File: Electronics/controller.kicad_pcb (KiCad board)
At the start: 2 copper layers, 70 x 50 mm, 21 parts, among them J101 Conn_01x06_Female, J102 Conn_01x06_Female, Q101 2N7002, Q102 2N7002, Q103 IRF9540NPBF, Q104 IRF9540NPBF

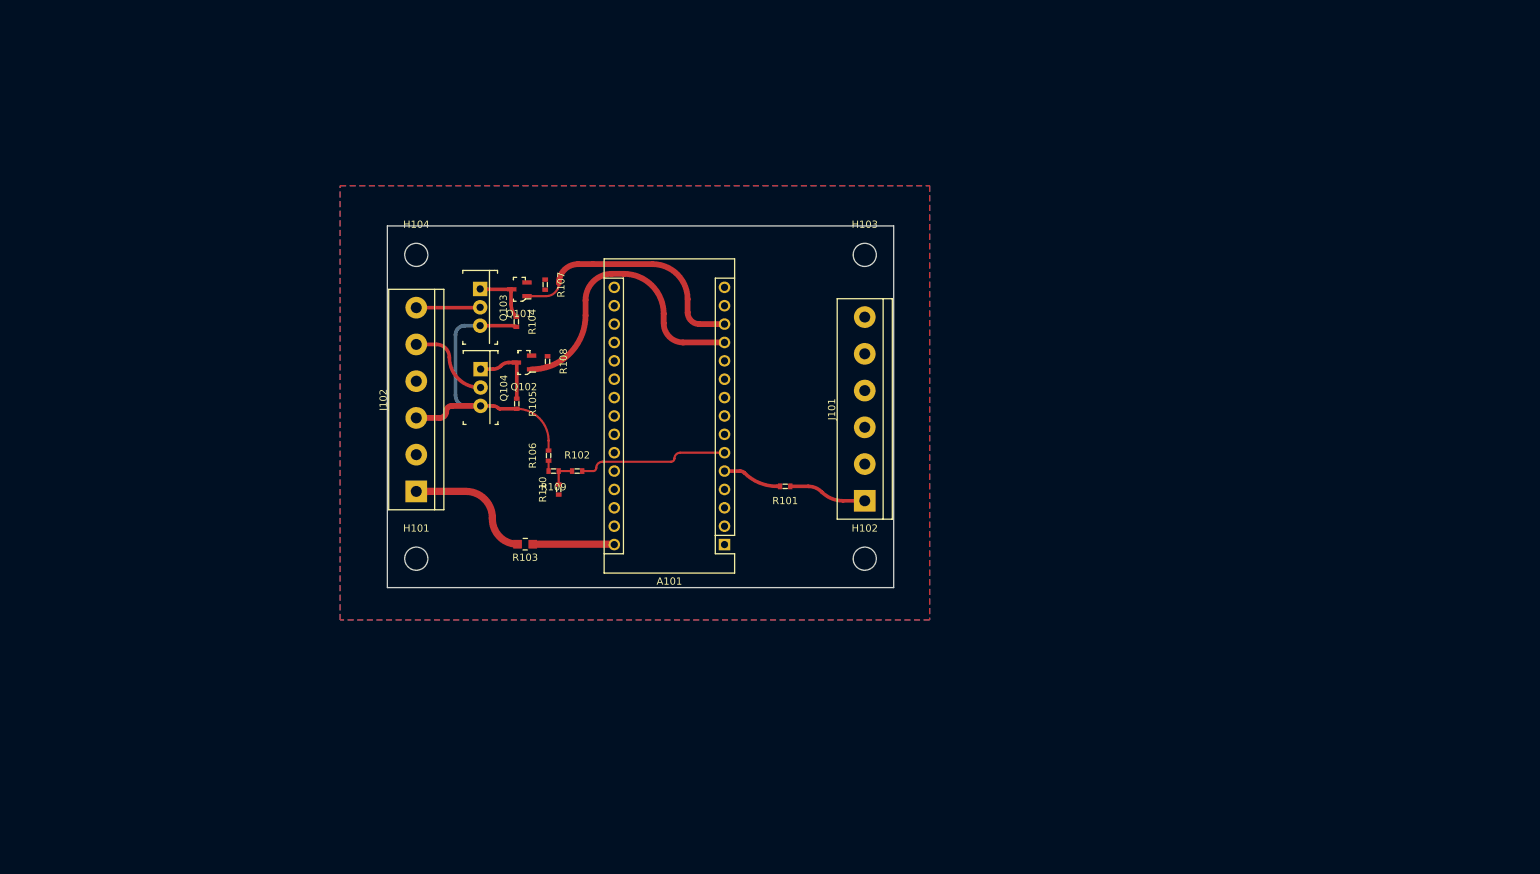
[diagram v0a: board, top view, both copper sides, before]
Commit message: Added third half bridge for BLDC applications
Signed-off-by: Finder <aki.kuusela@findersee.fi>
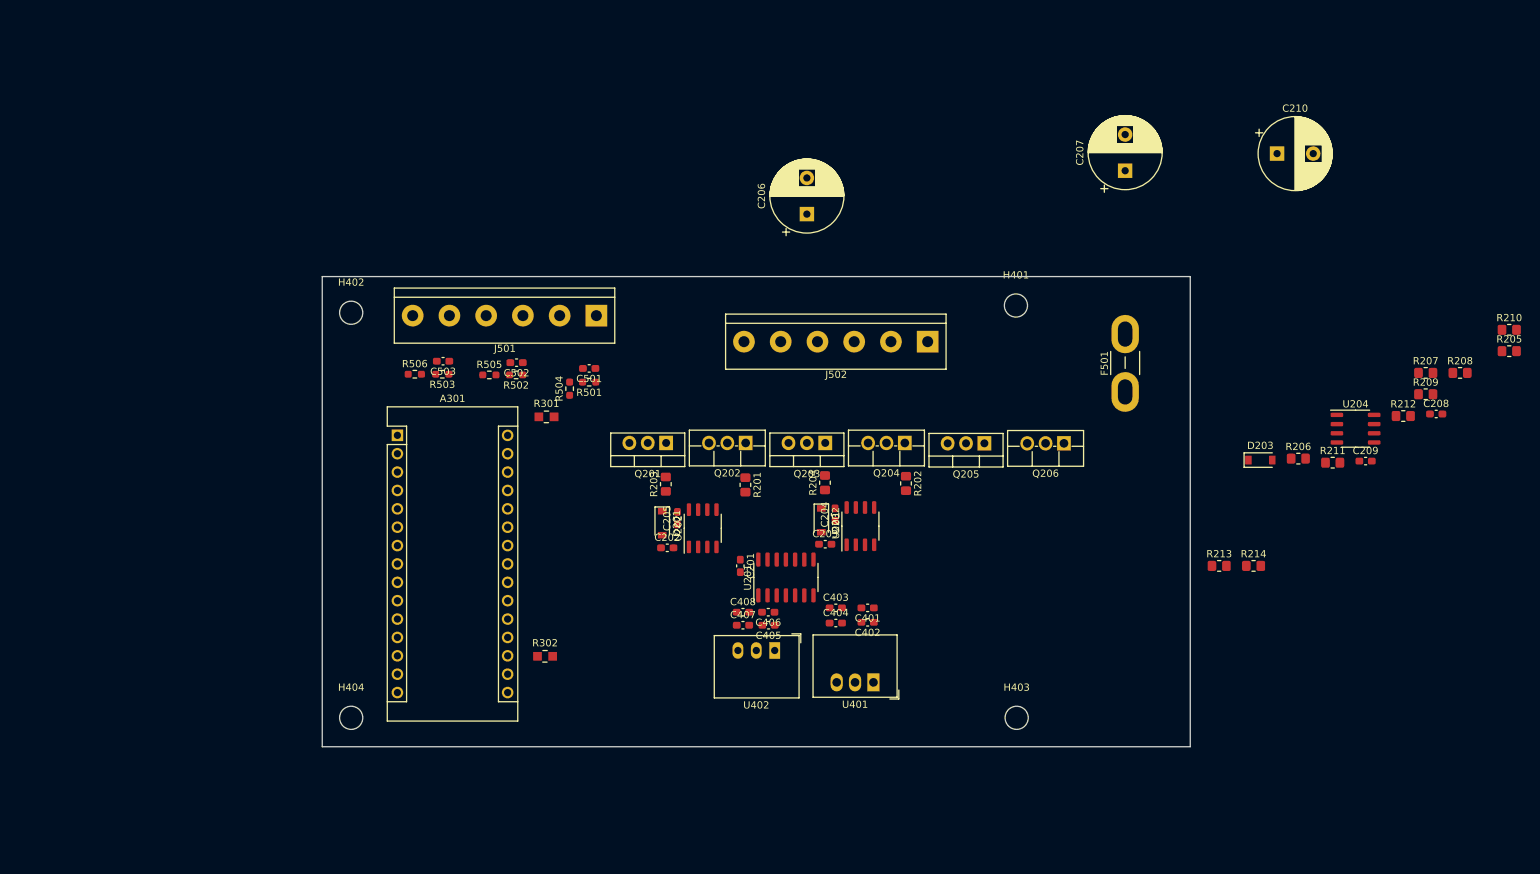
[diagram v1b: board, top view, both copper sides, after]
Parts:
- removed A101: Arduino_Nano_Every, Module:Arduino_Nano
- removed H101, H102, H103, H104: MountingHole, MountingHole:MountingHole_3.2mm_M3
- removed J101, J102: Conn_01x06_Female, TerminalBlock:TerminalBlock_bornier-6_P5.08mm
- removed Q101, Q102: 2N7002, digikey-footprints:SOT-23-3
- removed Q103, Q104: IRF9540NPBF, digikey-footprints:TO-220-3
- removed R101, R102: 1k, digikey-footprints:0603
- removed R103: 0r, digikey-footprints:0805
- removed R104, R105, R106, R107, R108, R109, R110: 10k, digikey-footprints:0603
- added A301: Arduino_Nano_Every, Module:Arduino_Nano, F.Cu at (81.4, 89.0)
- added C201: C, Capacitor_SMD:C_0603_1608Metric_Pad1.08x0.95mm_HandSolder, F.Cu at (128.8, 107.0)
- added C202: C, Capacitor_SMD:C_0603_1608Metric_Pad1.08x0.95mm_HandSolder, F.Cu at (118.7, 104.5)
- added C203: C, Capacitor_SMD:C_0603_1608Metric_Pad1.08x0.95mm_HandSolder, F.Cu at (140.5, 104.0)
- added C204: C, Capacitor_SMD:C_0603_1608Metric_Pad1.08x0.95mm_HandSolder, F.Cu at (141.9, 99.9)
- added C205: C, Capacitor_SMD:C_0603_1608Metric_Pad1.08x0.95mm_HandSolder, F.Cu at (120.1, 100.4)
- added C206: C, Capacitor_THT:CP_Radial_D10.0mm_P5.00mm, F.Cu at (138.0, 58.4)
- added C207: C, Capacitor_THT:CP_Radial_D10.0mm_P5.00mm, F.Cu at (182.0, 52.4)
- added C208: C, Capacitor_SMD:C_0603_1608Metric_Pad1.08x0.95mm_HandSolder, F.Cu at (225.0, 86.0)
- added C209: C, Capacitor_SMD:C_0603_1608Metric_Pad1.08x0.95mm_HandSolder, F.Cu at (215.2, 92.5)
- added C210: C, Capacitor_THT:CP_Radial_D10.0mm_P5.00mm, F.Cu at (203.0, 50.0)
- added C401: C, Capacitor_SMD:C_0603_1608Metric_Pad1.08x0.95mm_HandSolder, F.Cu at (146.4, 112.8)
- added C402: C, Capacitor_SMD:C_0603_1608Metric_Pad1.08x0.95mm_HandSolder, F.Cu at (146.4, 114.8)
- added C403: C, Capacitor_SMD:C_0603_1608Metric_Pad1.08x0.95mm_HandSolder, F.Cu at (142.0, 112.8)
- added C404: C, Capacitor_SMD:C_0603_1608Metric_Pad1.08x0.95mm_HandSolder, F.Cu at (142.0, 114.9)
- added C405: C, Capacitor_SMD:C_0603_1608Metric_Pad1.08x0.95mm_HandSolder, F.Cu at (132.7, 115.2)
- added C406: C, Capacitor_SMD:C_0603_1608Metric_Pad1.08x0.95mm_HandSolder, F.Cu at (132.7, 113.4)
- added C407: C, Capacitor_SMD:C_0603_1608Metric_Pad1.08x0.95mm_HandSolder, F.Cu at (129.2, 115.2)
- added C408: C, Capacitor_SMD:C_0603_1608Metric_Pad1.08x0.95mm_HandSolder, F.Cu at (129.2, 113.4)
- added C501: 100n, Capacitor_SMD:C_0603_1608Metric_Pad1.08x0.95mm_HandSolder, F.Cu at (107.9, 79.7)
- added C502: 100n, Capacitor_SMD:C_0603_1608Metric_Pad1.08x0.95mm_HandSolder, F.Cu at (97.9, 78.9)
- added C503: 100n, Capacitor_SMD:C_0603_1608Metric_Pad1.08x0.95mm_HandSolder, F.Cu at (87.7, 78.7)
- added D201: 1N5819, Diode_SMD:D_SOD-123, F.Cu at (118.0, 101.1)
- added D202: 1N5819, Diode_SMD:D_SOD-123, F.Cu at (140.0, 100.7)
- added D203: 1N5819, Diode_SMD:D_SOD-123, F.Cu at (200.7, 92.4)
- added F501: 20A, Fuse:Fuse_Blade_Mini_directSolder, F.Cu at (182.0, 83.0)
- added H401: MountingHole, MountingHole:MountingHole_3.2mm_M3, F.Cu at (166.9, 71.0)
- added H402: MountingHole, MountingHole:MountingHole_3.2mm_M3, F.Cu at (75.0, 72.0)
- added H403: MountingHole, MountingHole:MountingHole_3.2mm_M3, F.Cu at (167.0, 128.0)
- added H404: MountingHole, MountingHole:MountingHole_3.2mm_M3, F.Cu at (75.0, 128.0)
- added J501: Conn_01x06_Female, TerminalBlock:TerminalBlock_bornier-6_P5.08mm, F.Cu at (108.9, 72.4)
- added J502: Conn_01x06_Female, TerminalBlock:TerminalBlock_bornier-6_P5.08mm, F.Cu at (154.7, 76.0)
- added Q201: IRLZ44N, Package_TO_SOT_THT:TO-220-3_Vertical, F.Cu at (118.5, 90.0)
- added Q202: IRLIZ44N, Package_TO_SOT_THT:TO-220F-3_Vertical, F.Cu at (129.5, 90.0)
- added Q203: IRLZ44N, Package_TO_SOT_THT:TO-220-3_Vertical, F.Cu at (140.5, 90.0)
- added Q204: IRLIZ44N, Package_TO_SOT_THT:TO-220F-3_Vertical, F.Cu at (151.5, 90.0)
- added Q205: IRLZ44N, Package_TO_SOT_THT:TO-220-3_Vertical, F.Cu at (162.5, 90.1)
- added Q206: IRLIZ44N, Package_TO_SOT_THT:TO-220F-3_Vertical, F.Cu at (173.5, 90.1)
- added R201: 10, Resistor_SMD:R_0805_2012Metric_Pad1.20x1.40mm_HandSolder, F.Cu at (129.5, 95.8)
- added R202: 10, Resistor_SMD:R_0805_2012Metric_Pad1.20x1.40mm_HandSolder, F.Cu at (151.7, 95.6)
- added R203: 10, Resistor_SMD:R_0805_2012Metric_Pad1.20x1.40mm_HandSolder, F.Cu at (118.5, 95.7)
- added R204: 10, Resistor_SMD:R_0805_2012Metric_Pad1.20x1.40mm_HandSolder, F.Cu at (140.5, 95.5)
- added R205: 10k, Resistor_SMD:R_0805_2012Metric_Pad1.20x1.40mm_HandSolder, F.Cu at (235.1, 77.3)
- added R206: 10k, Resistor_SMD:R_0805_2012Metric_Pad1.20x1.40mm_HandSolder, F.Cu at (205.9, 92.2)
- added R207: 10k, Resistor_SMD:R_0805_2012Metric_Pad1.20x1.40mm_HandSolder, F.Cu at (223.6, 80.3)
- added R208: 10k, Resistor_SMD:R_0805_2012Metric_Pad1.20x1.40mm_HandSolder, F.Cu at (228.3, 80.3)
- added R209: 10, Resistor_SMD:R_0805_2012Metric_Pad1.20x1.40mm_HandSolder, F.Cu at (223.6, 83.3)
- added R210: 10, Resistor_SMD:R_0805_2012Metric_Pad1.20x1.40mm_HandSolder, F.Cu at (235.1, 74.4)
- added R211: 10k, Resistor_SMD:R_0805_2012Metric_Pad1.20x1.40mm_HandSolder, F.Cu at (210.7, 92.7)
- added R212: 10k, Resistor_SMD:R_0805_2012Metric_Pad1.20x1.40mm_HandSolder, F.Cu at (220.4, 86.3)
- added R213: 0, Resistor_SMD:R_0805_2012Metric_Pad1.20x1.40mm_HandSolder, F.Cu at (195.0, 107.0)
- added R214: 0, Resistor_SMD:R_0805_2012Metric_Pad1.20x1.40mm_HandSolder, F.Cu at (199.8, 107.0)
- added R301: 0r, digikey-footprints:0805, F.Cu at (102.0, 86.4)
- added R302: 0r, digikey-footprints:0805, F.Cu at (101.8, 119.5)
- added R501: 100, Resistor_SMD:R_0603_1608Metric_Pad0.98x0.95mm_HandSolder, F.Cu at (107.9, 81.6)
- added R502: 100, Resistor_SMD:R_0603_1608Metric_Pad0.98x0.95mm_HandSolder, F.Cu at (97.8, 80.6)
- added R503: 100, Resistor_SMD:R_0603_1608Metric_Pad0.98x0.95mm_HandSolder, F.Cu at (87.6, 80.5)
- added R504: 11k, Resistor_SMD:R_0603_1608Metric_Pad0.98x0.95mm_HandSolder, F.Cu at (105.2, 82.5)
- added R505: 11k, Resistor_SMD:R_0603_1608Metric_Pad0.98x0.95mm_HandSolder, F.Cu at (94.1, 80.6)
- added R506: 11k, Resistor_SMD:R_0603_1608Metric_Pad0.98x0.95mm_HandSolder, F.Cu at (83.8, 80.5)
- added U201: 74LS08, Package_SO:SO-14_3.9x8.65mm_P1.27mm, F.Cu at (135.1, 108.6)
- added U202: IR2101, Package_SO:SO-8_3.9x4.9mm_P1.27mm, F.Cu at (123.6, 101.8)
- added U203: IR2101, Package_SO:SO-8_3.9x4.9mm_P1.27mm, F.Cu at (145.4, 101.5)
- added U204: IR2101, Package_SO:SO-8_3.9x4.9mm_P1.27mm, F.Cu at (213.8, 88.0)
- added U401: R-78B15-2.0, Converter_DCDC:Converter_DCDC_RECOM_R-78B-2.0_THT, F.Cu at (147.2, 123.1)
- added U402: R-78E3.3-1.0, Converter_DCDC:Converter_DCDC_RECOM_R-78E-0.5_THT, F.Cu at (133.5, 118.7)
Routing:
- net +12P: track 44.7 -> 0.00 mm
- net Net-(A101-Pad12): track 40.3 -> 0.00 mm
- net Net-(A101-Pad13): track 34.9 -> 0.00 mm
- net Net-(A101-Pad6): track 21.0 -> 0.00 mm
- net +12V: track 18.0 -> 0.00 mm
- net Net-(J102-Pad5): track 12.1 -> 0.00 mm
- net Net-(A101-Pad30): track 11.3 -> 0.00 mm
- net Net-(J101-Pad1): track 10.8 -> 0.00 mm
- net Net-(Q102-Pad3): track 10.2 -> 0.00 mm
- net Net-(J102-Pad6): track 8.86 -> 0.00 mm
- net Net-(Q101-Pad3): track 8.39 -> 0.00 mm
- net Net-(A101-Pad5): track 8.22 -> 0.00 mm
- net Net-(R102-Pad1): track 3.70 -> 0.00 mm
- net Net-(R106-Pad1): track 1.44 -> 0.00 mm
- removed copper zone on B.Cu, net GND
- removed copper zone on F.Cu, net GND
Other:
- board size 70 x 50 mm -> 120 x 65 mm

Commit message: Layout update
Signed-off-by: Aki Kuusela <git@findersee.fi>
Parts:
- removed U401: R-78B15-2.0, Converter_DCDC:Converter_DCDC_RECOM_R-78B-2.0_THT
- added C301: 100n, Capacitor_SMD:C_0603_1608Metric_Pad1.08x0.95mm_HandSolder, F.Cu at (111.3, 62.4)
- added U1: R-78C15-1.0, Converter_DCDC:Converter_DCDC_RECOM_R-78E-0.5_THT, F.Cu at (136.4, 122.9)
- added U301: 74HC86, Package_SO:SO-14_3.9x8.65mm_P1.27mm, F.Cu at (109.7, 68.0)
- H401, H402, H403, H404: footprint MountingHole:MountingHole_3.2mm_M3 -> MountingHole:MountingHole_4mm
- J501: moved to B.Cu
- J502: value Conn_01x06_Female -> Motor Con; moved to B.Cu
- moved R210 95.7 mm to (146.4, 110.2)
- moved C208 89.9 mm to (137.4, 106.2), turned to -90 degrees
- moved R205 88.1 mm to (147.2, 71.9), turned to -90 degrees
- moved R209 85.5 mm to (146.3, 119.9), turned to 180 degrees
- moved R214 83.6 mm to (120.3, 81.0), turned to 90 degrees
- moved R213 81.8 mm to (117.4, 81.0), turned to 90 degrees
- moved R208 80.8 mm to (147.5, 83.0), turned to 90 degrees
- moved R207 78.6 mm to (147.4, 61.0), turned to -90 degrees
- moved U204 76.9 mm to (140.4, 110.9)
- moved R212 75.4 mm to (147.4, 105.0), turned to 90 degrees
- moved R501 75.2 mm to (41.8, 117.4)
- moved C501 75.2 mm to (41.8, 115.5)
- moved R301 75.2 mm to (35.9, 122.2)
- moved R504 75.2 mm to (39.1, 118.3)
- moved C209 74.9 mm to (141.8, 107.4)
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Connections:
- J502 pad 1: Net-(F501-Pad2) -> /Connectors/MOTOR POS
- J502 pad 2: GND -> /Connectors/MOTOR NEG
- J502 pad 3: unconnected-(J502-Pad3) -> /Connectors/MOTOR C
- J502 pad 4: /Connectors/MOTOR C -> unconnected-(J502-Pad4)
- J502 pad 5: /Connectors/MOTOR NEG -> GND
- J502 pad 6: /Connectors/MOTOR POS -> Net-(F501-Pad2)
- U201 pad 10: +3V3 -> /Connectors/Limit 2
- U201 pad 11: Net-(U201-Pad11) -> unconnected-(U201-Pad11)
- U201 pad 12: /Hbridge/HIN C -> +3V3
- U201 pad 13: /Hbridge/C LIMIT -> +3V3
- U201 pad 4: /Hbridge/HIN B -> /Hbridge/HIN C
- U201 pad 5: /Connectors/Limit 2 -> /Hbridge/C LIMIT
- U201 pad 8: unconnected-(U201-Pad8) -> Net-(U201-Pad8)
- U201 pad 9: +3V3 -> /Hbridge/HIN B
- U203 pad 2: Net-(U201-Pad6) -> Net-(U201-Pad8)
- U204 pad 2: Net-(U201-Pad11) -> Net-(U201-Pad6)
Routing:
- net /Connectors/Limit 2: track 0.00 -> 75.4 mm, vias 0 -> 1
- net VCC: track 0.00 -> 75.1 mm
- net /Hbridge/LIN A: track 0.00 -> 67.0 mm, vias 0 -> 2
- net /Hbridge/C LIMIT: track 0.00 -> 65.8 mm, vias 0 -> 1
- net /Connectors/Limit 1: track 0.00 -> 61.8 mm, vias 0 -> 1
- net /Hbridge/HIN C: track 0.00 -> 58.0 mm
- net /Hbridge/HIN A: track 0.00 -> 55.0 mm
- net /Hbridge/HIN B: track 0.00 -> 54.1 mm, vias 0 -> 2
- net +3V3: track 0.00 -> 45.3 mm
- net /Hbridge/LIN C: track 0.00 -> 41.8 mm
- net Vdrive: track 0.00 -> 41.1 mm
- net Net-(U201-Pad6): track 0.00 -> 32.4 mm
- net /Connectors/MOTOR POS: track 0.00 -> 21.5 mm
- net /Connectors/MOTOR C: track 0.00 -> 21.4 mm
- net Net-(U201-Pad3): track 0.00 -> 21.0 mm
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- added copper zone on B.Cu, net /Connectors/MOTOR C
- added copper zone on B.Cu, net /Connectors/MOTOR NEG
- added copper zone on B.Cu, net /Connectors/MOTOR POS
- added copper zone on B.Cu, net GND
- added copper zone on F.Cu, net GND
- added copper zone on F.Cu, net Vdrive
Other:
- board size 120 x 65 mm -> 100 x 75 mm

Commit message: Added hall sensor circuitry
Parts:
- added C504: 10n, Capacitor_SMD:C_0603_1608Metric_Pad1.08x0.95mm_HandSolder, F.Cu at (47.4, 62.8)
- added C505: 10n, Capacitor_SMD:C_0603_1608Metric_Pad1.08x0.95mm_HandSolder, F.Cu at (38.7, 67.8)
- added C506: 10n, Capacitor_SMD:C_0603_1608Metric_Pad1.08x0.95mm_HandSolder, F.Cu at (38.7, 75.3)
- added C507: 10n, Capacitor_SMD:C_0603_1608Metric_Pad1.08x0.95mm_HandSolder, F.Cu at (38.7, 62.8)
- added C508: 10n, Capacitor_SMD:C_0603_1608Metric_Pad1.08x0.95mm_HandSolder, F.Cu at (38.7, 65.3)
- added C509: 10n, Capacitor_SMD:C_0603_1608Metric_Pad1.08x0.95mm_HandSolder, F.Cu at (43.0, 67.8)
- added J503: Conn_01x05_Female, Connector_PinHeader_2.54mm:PinHeader_1x05_P2.54mm_Vertical, F.Cu at (34.2, 63.9)
- added R303: 0r, digikey-footprints:0805, F.Cu at (59.9, 63.0)
- added R507: 100, Resistor_SMD:R_0603_1608Metric_Pad0.98x0.95mm_HandSolder, F.Cu at (38.7, 70.3)
- added R508: 100, Resistor_SMD:R_0603_1608Metric_Pad0.98x0.95mm_HandSolder, F.Cu at (38.7, 72.8)
- added R509: 100, Resistor_SMD:R_0603_1608Metric_Pad0.98x0.95mm_HandSolder, F.Cu at (47.4, 65.3)
- added R510: 8k2, Resistor_SMD:R_0603_1608Metric_Pad0.98x0.95mm_HandSolder, F.Cu at (43.0, 62.8)
- added R511: 8k2, Resistor_SMD:R_0603_1608Metric_Pad0.98x0.95mm_HandSolder, F.Cu at (43.0, 65.3)
- added R512: 8k2, Resistor_SMD:R_0603_1608Metric_Pad0.98x0.95mm_HandSolder, F.Cu at (51.8, 62.8)
- C202, C203, C208: value C -> 1u
- C204, C205, C209: value C -> 10u
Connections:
- net +3V3 renamed VDD
- A301 pad 10: unconnected-(A301-Pad10) -> /MCU/HALL A
- A301 pad 11: unconnected-(A301-Pad11) -> /MCU/HALL B
- A301 pad 27: unconnected-(A301-Pad27) -> Net-(A301-Pad27)
- A301 pad 7: unconnected-(A301-Pad7) -> /MCU/HALL C
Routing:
- net /Hbridge/HIN B: track 54.1 -> 86.1 mm, vias 2 -> 3
